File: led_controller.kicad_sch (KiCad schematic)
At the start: 20 parts, among them SW1 Toggle switch, SW2 Toggle switch, SW3 Toggle switch, SW4 Toggle switch

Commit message: add motor
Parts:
- added M1: Motor_DC, symbol Motor:Motor_DC
- added RV1: R_Potentiometer, symbol Device:R_Potentiometer
- added SW5: Toggle switch, symbol Switch:SW_SPST
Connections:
- net at C1.1, C3.1, SW1.1 (A)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: now also SW5.2 (B)
- net at A1.29 (GND), A1.4 (GND), BT1.2 (-)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: now also M1.2 (-)
- new net: M1.1 (+), RV1.3
- new net: RV1.1, SW5.1 (A)
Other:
- moved on the sheet: A1, BT1, C1, C2, C3, C4, C5, C6, D1, D2, D3, D4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

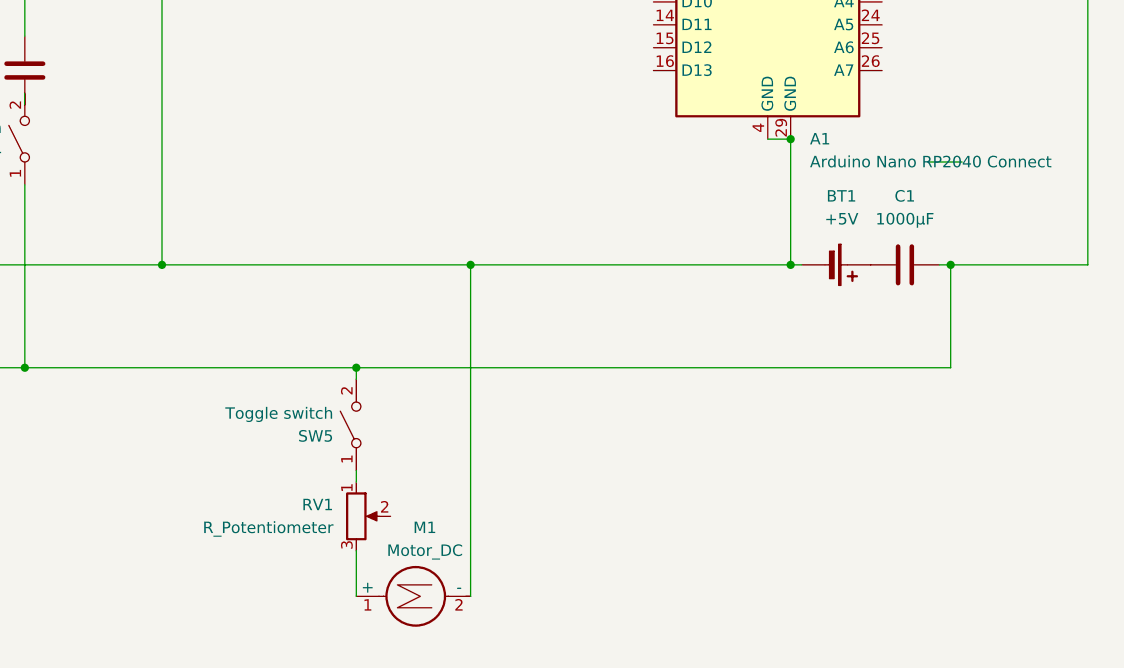
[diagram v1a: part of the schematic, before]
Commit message: add values for potentiometer and motor
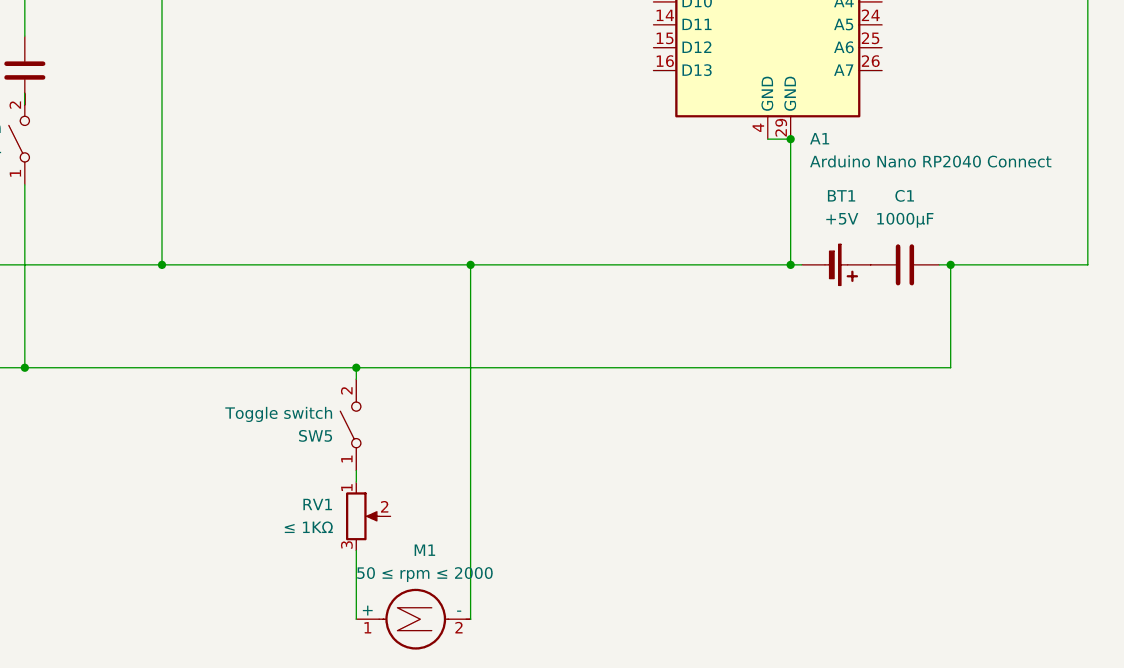
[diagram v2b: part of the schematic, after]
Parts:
- M1: value Motor_DC -> 50 ≤ rpm ≤ 2000
- RV1: value R_Potentiometer -> ≤ 1KΩ
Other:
- moved on the sheet: M1
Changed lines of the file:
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@@
 	(wire
 		(pts
-			(xy 191.77 107.95) (xy 191.77 144.78)
+			(xy 191.77 107.95) (xy 191.77 147.32)
 		)
 		(stroke
@@
 	(wire
 		(pts
-			(xy 242.57 96.52) (xy 246.38 96.52)
-		)
-		(stroke
-			(width 0)
-			(type default)
-		)
-	)
-	(wire
-		(pts
 			(xy 157.48 68.58) (xy 157.48 107.95)
 		)
@@
 	(wire
 		(pts
-			(xy 179.07 139.7) (xy 179.07 144.78)
+			(xy 179.07 139.7) (xy 179.07 147.32)
 		)
 		(stroke
@@
 	(symbol
 		(lib_id "Motor:Motor_DC")
-		(at 184.15 144.78 90)
+		(at 184.15 147.32 90)
 		(unit 1)
 		(exclude_from_sim no)
@@
 		(dnp no)
 		(property "Reference" "M1"
-			(at 186.69 137.16 90)
-			(effects
-				(font
-					(size 1.27 1.27)
-				)
-			)
-		)
-		(property "Value" "Motor_DC"
 			(at 186.69 139.7 90)
 			(effects
@@
 			)
 		)
+		(property "Value" "50 ≤ rpm ≤ 2000"
+			(at 186.69 142.24 90)
+			(effects
+				(font
+					(size 1.27 1.27)
+				)
+			)
+		)
 		(property "Footprint" ""
-			(at 186.436 144.78 0)
+			(at 186.436 147.32 0)
 			(effects
 				(font
@@
 		)
 		(property "Datasheet" "~"
-			(at 186.436 144.78 0)
+			(at 186.436 147.32 0)
 			(effects
 				(font
@@
 		)
 		(property "Description" "DC Motor"
-			(at 184.15 144.78 0)
+			(at 184.15 147.32 0)
 			(effects
 				(font
@@
 			)
 		)
-		(property "Value" "R_Potentiometer"
+		(property "Value" "≤ 1KΩ"
 			(at 176.53 137.1599 0)
 			(effects

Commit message: add push button
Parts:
- removed SW5: Toggle switch, symbol Switch:SW_SPST
- added R5: 10KΩ, symbol Device:R
- added SW5, SW6: SW_Push, symbol Switch:SW_Push
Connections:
- net at C1.1, C3.1, SW1.1 (A)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: now also SW5.2, SW6.1
- net at A1.29 (GND), A1.4 (GND), BT1.2 (-)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: now also R5.2
- net at A1.16 (D13): now also R5.1, SW6.2
- net at RV1.1: now also SW5.1
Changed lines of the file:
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@@
+	)
+	(junction
+		(at 204.47 93.98)
+		(diameter 0)
+		(color 0 0 0 0)
 	)
 	(junction
@@
 	)
 	(junction
+		(at 204.47 119.38)
+		(diameter 0)
+		(color 0 0 0 0)
+	)
+	(junction
 		(at 227.33 107.95)
 		(diameter 0)
@@
 	(wire
 		(pts
+			(xy 212.09 86.36) (xy 204.47 86.36)
+		)
+		(stroke
+			(width 0)
+			(type default)
+		)
+	)
+	(wire
+		(pts
 			(xy 177.8 49.53) (xy 177.8 66.04)
 		)
@@
 	(wire
 		(pts
+			(xy 204.47 104.14) (xy 204.47 119.38)
+		)
+		(stroke
+			(width 0)
+			(type default)
+		)
+	)
+	(wire
+		(pts
 			(xy 78.74 68.58) (xy 78.74 82.55)
 		)
@@
 	(wire
 		(pts
+			(xy 157.48 107.95) (xy 191.77 107.95)
+		)
+		(stroke
+			(width 0)
+			(type default)
+		)
+	)
+	(wire
+		(pts
+			(xy 191.77 93.98) (xy 204.47 93.98)
+		)
+		(stroke
+			(width 0)
+			(type default)
+		)
+	)
+	(wire
+		(pts
+			(xy 191.77 95.25) (xy 191.77 93.98)
+		)
+		(stroke
+			(width 0)
+			(type default)
+		)
+	)
+	(wire
+		(pts
 			(xy 229.87 30.48) (xy 260.35 30.48)
 		)
@@
 	(wire
 		(pts
-			(xy 157.48 107.95) (xy 191.77 107.95)
-		)
-		(stroke
-			(width 0)
-			(type default)
-		)
-	)
-	(wire
-		(pts
 			(xy 142.24 88.9) (xy 142.24 90.17)
 		)
@@
 	(wire
 		(pts
+			(xy 204.47 86.36) (xy 204.47 93.98)
+		)
+		(stroke
+			(width 0)
+			(type default)
+		)
+	)
+	(wire
+		(pts
 			(xy 54.61 57.15) (xy 54.61 60.96)
 		)
@@
 	(wire
 		(pts
+			(xy 191.77 102.87) (xy 191.77 107.95)
+		)
+		(stroke
+			(width 0)
+			(type default)
+		)
+	)
+	(wire
+		(pts
+			(xy 204.47 119.38) (xy 245.11 119.38)
+		)
+		(stroke
+			(width 0)
+			(type default)
+		)
+	)
+	(wire
+		(pts
 			(xy 157.48 68.58) (xy 157.48 107.95)
 		)
@@
 	(wire
 		(pts
-			(xy 179.07 119.38) (xy 245.11 119.38)
+			(xy 179.07 119.38) (xy 204.47 119.38)
 		)
 		(stroke
@@
 	)
 	(symbol
+		(lib_id "Device:R")
+		(at 191.77 99.06 0)
+		(unit 1)
+		(exclude_from_sim no)
+		(in_bom yes)
+		(on_board yes)
+		(dnp no)
+		(fields_autoplaced yes)
+		(property "Reference" "R5"
+			(at 194.31 97.7899 0)
+			(effects
+				(font
+					(size 1.27 1.27)
+				)
+				(justify left)
+			)
+		)
+		(property "Value" "10KΩ"
+			(at 194.31 100.3299 0)
+			(effects
+				(font
+					(size 1.27 1.27)
+				)
+				(justify left)
+			)
+		)
+		(property "Footprint" ""
+			(at 189.992 99.06 90)
+			(effects
+				(font
+					(size 1.27 1.27)
+				)
+				(hide yes)
+			)
+		)
+		(property "Datasheet" "~"
+			(at 191.77 99.06 0)
+			(effects
+				(font
+					(size 1.27 1.27)
+				)
+				(hide yes)
+			)
+		)
+		(property "Description" "Resistor"
+			(at 191.77 99.06 0)
+			(effects
+				(font
+					(size 1.27 1.27)
+				)
+				(hide yes)
+			)
+		)
+		(pin "2"
+		)
+		(pin "1"
+		)
+		(instances
+			(project ""
+				(path "/33db064c-d5ae-416f-86c1-c095f962d498"
+					(reference "R5")
+					(unit 1)
+				)
+			)
+		)
+	)
+	(symbol
+		(lib_id "Switch:SW_Push")
+		(at 179.07 125.73 90)
+		(unit 1)
+		(exclude_from_sim no)
+		(in_bom yes)
+		(on_board yes)
+		(dnp no)
+		(fields_autoplaced yes)
+		(property "Reference" "SW5"
+			(at 180.34 124.4599 90)
+			(effects
+				(font
+					(size 1.27 1.27)
+				)
+				(justify right)
+			)
+		)
+		(property "Value" "SW_Push"
+			(at 180.34 126.9999 90)
+			(effects
+				(font
+					(size 1.27 1.27)
+				)
+				(justify right)
+			)
+		)
+		(property "Footprint" ""
+			(at 173.99 125.73 0)
+			(effects
+				(font
+					(size 1.27 1.27)
+				)
+				(hide yes)
+			)
+		)
+		(property "Datasheet" "~"
+			(at 173.99 125.73 0)
+			(effects
+				(font
+					(size 1.27 1.27)
+				)
+				(hide yes)
+			)
+		)
+		(property "Description" "Push button switch, generic, two pins"
+			(at 179.07 125.73 0)
+			(effects
+				(font
+					(size 1.27 1.27)
+				)
+				(hide yes)
+			)
+		)
+		(pin "1"
+		)
+		(pin "2"
+		)
+		(instances
+			(project "led_controller"
+				(path "/33db064c-d5ae-416f-86c1-c095f962d498"
+					(reference "SW5")
+					(unit 1)
+				)
+			)
+		)
+	)
+	(symbol
 		(lib_id "Switch:SW_SPST")
 		(at 46.99 92.71 90)
@@
 	(symbol
 		(lib_id "Switch:SW_SPST")
-		(at 179.07 125.73 90)
-		(unit 1)
-		(exclude_from_sim no)
-		(in_bom yes)
-		(on_board yes)
-		(dnp no)
-		(property "Reference" "SW5"
-			(at 176.53 127.0001 90)
-			(effects
-				(font
-					(size 1.27 1.27)
-				)
-				(justify left)
-			)
-		)
-		(property "Value" "Toggle switch"
-			(at 176.53 124.4601 90)
-			(effects
-				(font
-					(size 1.27 1.27)
-				)
-				(justify left)
-			)
-		)
-		(property "Footprint" ""
-			(at 179.07 125.73 0)
-			(effects
-				(font
-					(size 1.27 1.27)
-				)
-				(hide yes)
-			)
-		)
-		(property "Datasheet" "~"
-			(at 179.07 125.73 0)
-			(effects
-				(font
-					(size 1.27 1.27)
-				)
-				(hide yes)
-			)
-		)
-		(property "Description" "Single Pole Single Throw (SPST) switch"
-			(at 179.07 125.73 0)
-			(effects
-				(font
-					(size 1.27 1.27)
-				)
-				(hide yes)
-			)
-		)
-		(pin "1"
-		)
-		(pin "2"
-		)
-		(instances
-			(project "led_controller"
-				(path "/33db064c-d5ae-416f-86c1-c095f962d498"
-					(reference "SW5")
-					(unit 1)
-				)
-			)
-		)
-	)
-	(symbol
-		(lib_id "Switch:SW_SPST")
 		(at 78.74 93.98 90)
 		(unit 1)
@@
 					(unit 1)
 				)
+			)
+		)
+	)
+	(symbol
+		(lib_id "Switch:SW_Push")
+		(at 204.47 99.06 90)
+		(unit 1)
+		(exclude_from_sim no)
+		(in_bom yes)
+		(on_board yes)
+		(dnp no)
+		(fields_autoplaced yes)
+		(property "Reference" "SW6"
+			(at 205.74 97.7899 90)
+			(effects
+				(font
+					(size 1.27 1.27)
+				)
+				(justify right)
+			)
+		)
+		(property "Value" "SW_Push"
+			(at 205.74 100.3299 90)
+			(effects
+				(font
+					(size 1.27 1.27)
+				)
+				(justify right)
+			)
+		)
+		(property "Footprint" ""
+			(at 199.39 99.06 0)
+			(effects
+				(font
+					(size 1.27 1.27)
+				)
+				(hide yes)
+			)
+		)
+		(property "Datasheet" "~"
+			(at 199.39 99.06 0)
+			(effects
+				(font
+					(size 1.27 1.27)
+				)
+				(hide yes)
+			)
+		)
+		(property "Description" "Push button switch, generic, two pins"
+			(at 204.47 99.06 0)
+			(effects
+				(font
+					(size 1.27 1.27)
+				)
+				(hide yes)
+			)
+		)
+		(pin "1"
+		)
+		(pin "2"
+		)
+		(instances
+			(project ""
+				(path "/33db064c-d5ae-416f-86c1-c095f962d498"
+					(reference "SW6")
+					(unit 1)
+				)

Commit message: fix switch
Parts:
- removed SW2, SW3, SW4: Toggle switch, symbol Switch:SW_SPST
- added SW7: Toggle switch, symbol Switch:SW_SPST
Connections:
- net at C1.1, C3.1, SW5.2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: now also SW7.1 (A); no longer SW1.1 (A)
- net at C2.1: now also C4.1, C5.1, C6.1, SW7.2 (B); no longer SW1.2 (B)
- net at C1.2: now also SW1.1 (A); no longer BT1.1 (+)
- new net: BT1.1 (+), SW1.2 (B)
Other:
- moved on the sheet: C1
